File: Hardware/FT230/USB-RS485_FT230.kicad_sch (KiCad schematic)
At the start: 35 parts, among them J1 USB_C_Receptacle_USB2.0_16P, J3 7-pin con, J4 Conn_02x03_Odd_Even, Q1 BC857, U1 FT230XQ, U4 DC-DC, U5 AP7345D-1833RH4-7, U6 SN75176, U7 ADuM121N

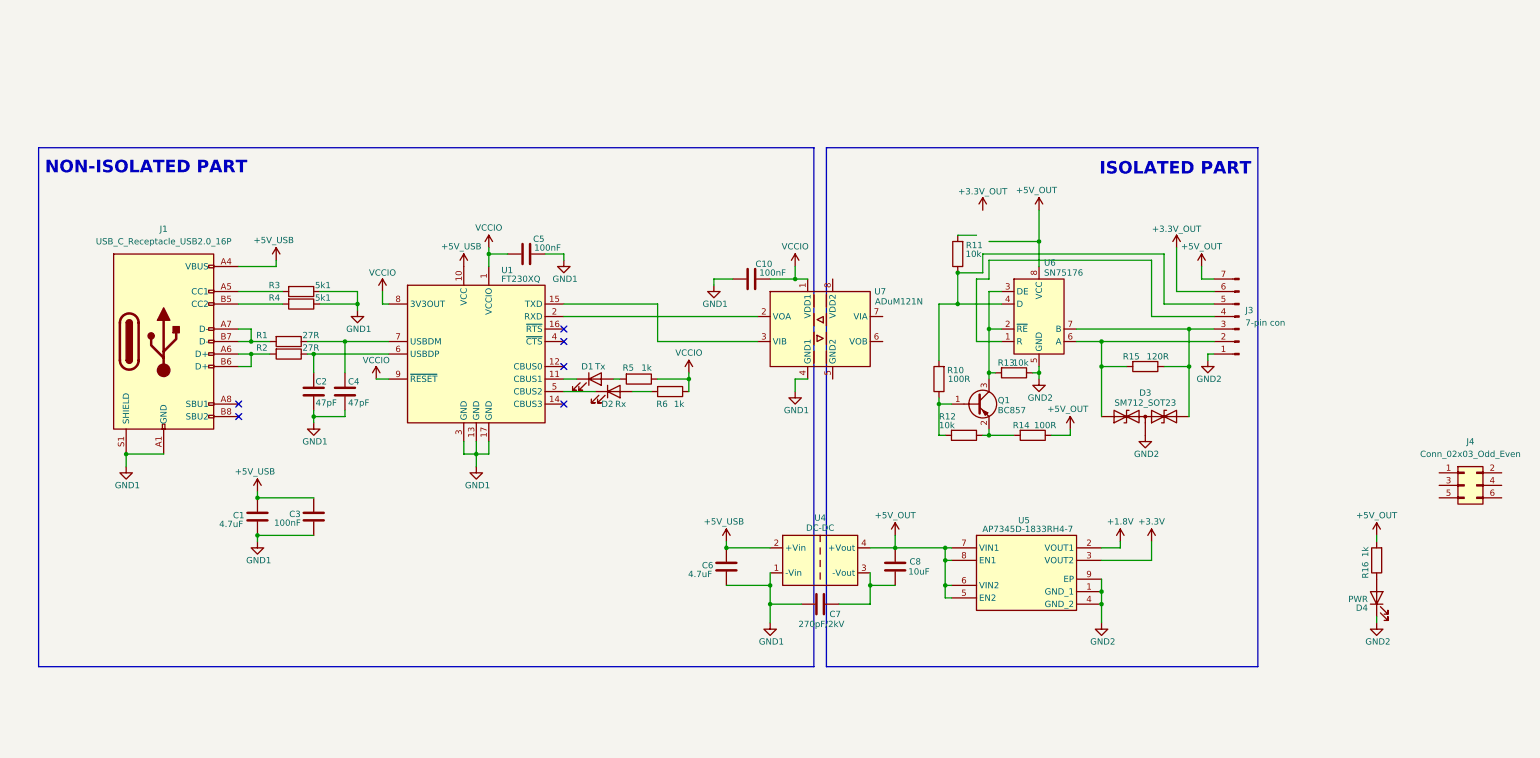
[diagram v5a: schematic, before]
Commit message: ADuM iteration. Readme.
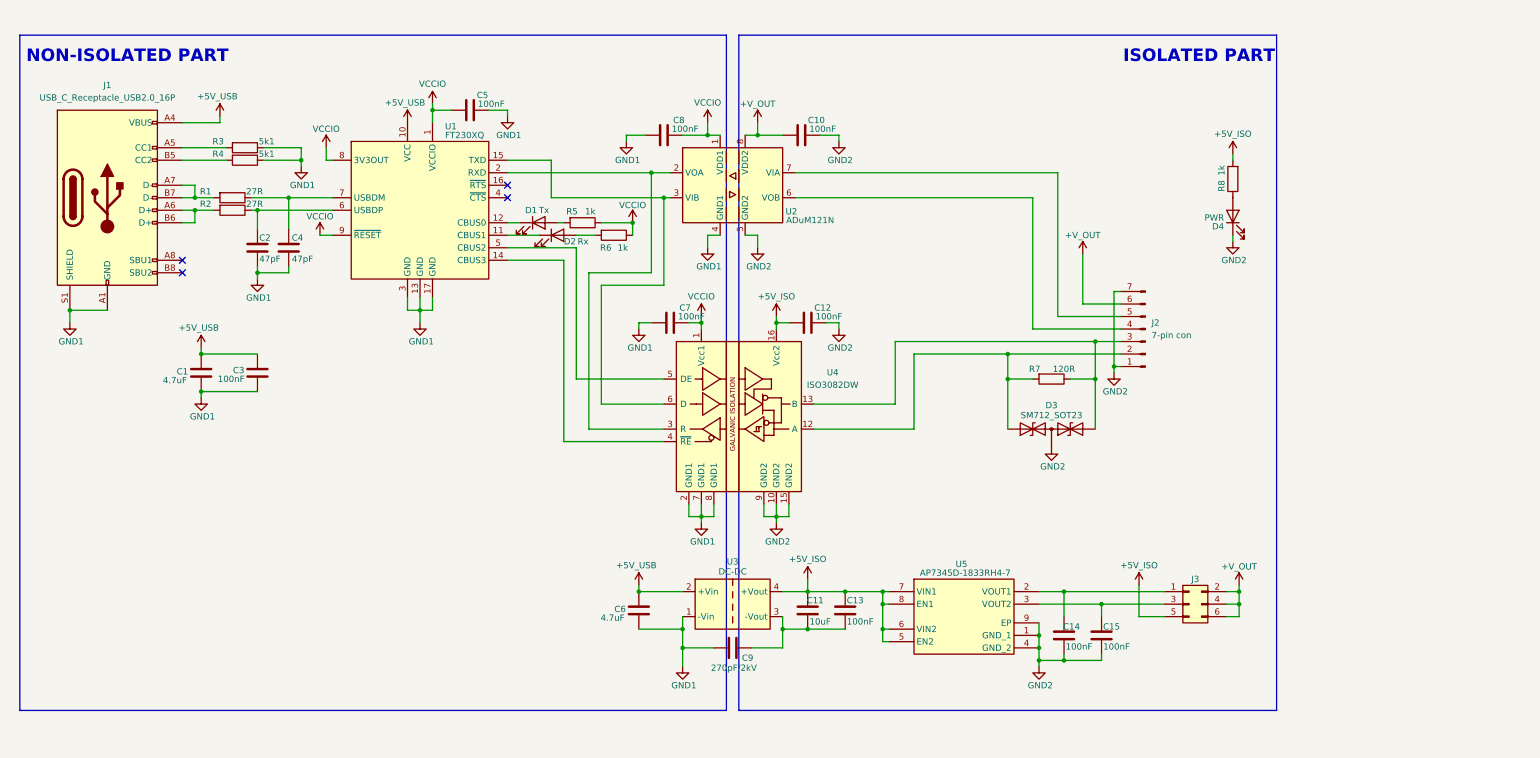
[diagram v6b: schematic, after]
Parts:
- removed Q1: BC857, Package_TO_SOT_SMD:SOT-23, symbol Transistor_BJT:BC857
- removed R10, R14: 100R, Resistor_SMD:R_0805_2012Metric, symbol Device:R
- removed R11, R12, R13: 10k, Resistor_SMD:R_0805_2012Metric, symbol Device:R
- removed U6: SN75176, Package_SO:SOIC-8_3.9x4.9mm_P1.27mm, symbol Interface_UART:SN75176AD
- added C10, C12, C13, C14, C15, C7: 100nF, Capacitor_SMD:C_0805_2012Metric, symbol Device:C
- added U4: ISO3082DW, Package_SO:SOIC-16W_7.5x10.3mm_P1.27mm, symbol Interface_UART:ISO3082DW
- renumbered C8 to C11, C10 to C8, C7 to C9, J3 to J2, J4 to J3, R15 to R7, R16 to R8, U7 to U2, U4 to U3
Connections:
- net +1.8V is gone; now on an unnamed net: U5.2 (VOUT1)
- net +3.3V is gone; now on an unnamed net: U5.3 (VOUT2)
- net +3.3V_OUT is gone; now on net +V_OUT: J2.6 (Pin_6)
- net GND1: now also C7.1, U4.2 (GND1), U4.7 (GND1), U4.8 (GND1)
- net GND2: now also J2.7 (Pin_7), U2.5 (GND2), C10.2, C12.2, C14.1, C15.1, U4.10 (GND2), U4.15 (GND2), U4.9 (GND2)
- net VCCIO: now also C7.2, U4.1 (Vcc1)
- net at D2.1 (K): now also U1.11 (CBUS1); no longer U1.5 (CBUS2)
- net at J2.5 (Pin_5): now also U2.7 (VIA)
- net at D3.1 (A1), J2.2 (Pin_2), R7.2: now also U4.12 (A)
- net at D3.2 (A2), J2.3 (Pin_3), R7.1: now also U4.13 (B)
- net at U1.2 (RXD), U2.2 (VOA): now also U4.3 (R)
- net at U1.15 (TXD), U2.3 (VIB): now also U4.6 (D)
- net at U2.6 (VOB): now also J2.4 (Pin_4)
- net +V_OUT: now reaches U2.8 (VDD2)
- net +V_OUT: now also J3.2 (Pin_2), J3.4 (Pin_4), J3.6 (Pin_6), C10.1
- net at D1.1 (K): now also U1.12 (CBUS0); no longer U1.11 (CBUS1)
- net at C11.1, C9.2, U3.3 (-Vout): now also C13.1
- net at J3.1 (Pin_1): now also C14.2
- net at J3.3 (Pin_3): now also C15.2
- net +5V_ISO: now reaches J3.5 (Pin_5)
- net +5V_ISO: now also C11.2, R8.2, U3.4 (+Vout), U5.5 (EN2), U5.6 (VIN2), U5.7 (VIN1), U5.8 (EN1), C12.1, C13.2, U4.16 (Vcc2)
- net at U1.14 (CBUS3): now also U4.4 (~{RE})
- removed net +5V_OUT: C11.2, J2.7 (Pin_7), R8.2, U3.4 (+Vout), U5.5 (EN2), U5.6 (VIN2), U5.7 (VIN1), U5.8 (EN1)
- new net: U1.5 (CBUS2), U4.5 (DE)
- no-connect marks 6 -> 4
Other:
- moved on the sheet: C1, C11, C2, C3, C4, C5, C6, C8, C9, D1, D2, D3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

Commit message: schematics update
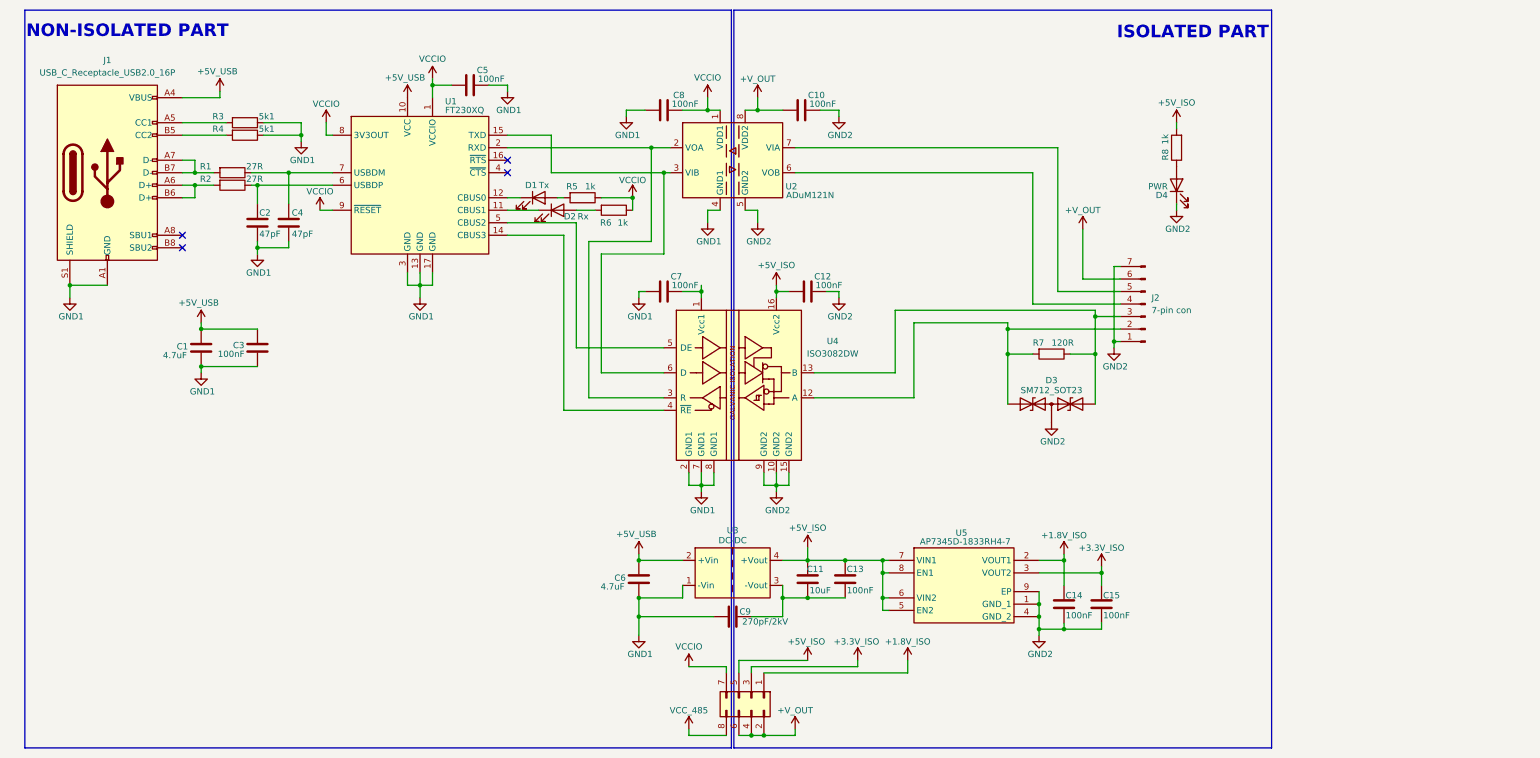
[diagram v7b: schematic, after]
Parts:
- removed J3: Conn_02x03_Odd_Even, Connector_PinHeader_1.00mm:PinHeader_2x03_P1.00mm_Vertical, symbol Connector_Generic:Conn_02x03_Odd_Even
- added J4: Conn_02x04_Odd_Even, symbol Connector_Generic:Conn_02x04_Odd_Even
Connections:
- net +5V_ISO: now also J4.5 (Pin_5)
- net +V_OUT: now also J4.2 (Pin_2), J4.4 (Pin_4), J4.6 (Pin_6)
- net VCCIO: now also J4.7 (Pin_7); no longer C7.2, U4.1 (Vcc1)
- net +3.3V_ISO: now reaches C15.2, U5.3 (VOUT2)
- net +3.3V_ISO: now also J4.3 (Pin_3)
- net +1.8V_ISO: now reaches C14.2, U5.2 (VOUT1)
- net +1.8V_ISO: now also J4.1 (Pin_1)
- new net: C7.2, U4.1 (Vcc1)
- new net VCC_485: J4.8 (Pin_8)
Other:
- moved on the sheet: C1, C10, C11, C12, C13, C14, C15, C2, C3, C4, C5, C6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

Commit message: Schematics update
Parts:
- added C16: 100nF, Capacitor_SMD:C_0805_2012Metric, symbol Device:C
- added U6: TS5A3159DCK, Package_TO_SOT_SMD:SOT-363_SC-70-6, symbol Analog_Switch:TS5A3159DCK
- J4: footprint (none) -> Connector_PinHeader_2.54mm:PinHeader_2x04_P2.54mm_Vertical
- U4: value ISO3082DW -> ISO3082DWR; MPN (none) -> ISO3082DWR; Manufacturer (none) -> Texas Instruments
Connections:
- net GND1: now also C16.2, U6.2 (GND)
- net VCCIO: now also C7.2, U4.1 (Vcc1), C16.1, U6.5 (V+)
- net VCC_485 renamed RS_ACT
- net RS_ACT: now also U6.6
- new net: U2.2 (VOA), U6.3
- new net: U4.3 (R), U6.1
- new net: U1.2 (RXD), U6.4
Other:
- moved on the sheet: C1, C10, C3, C8
